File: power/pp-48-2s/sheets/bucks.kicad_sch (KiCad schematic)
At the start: 38 parts, among them J4 12V AUX OUT, U1 LM5164DDA, U2 LM5164DDA

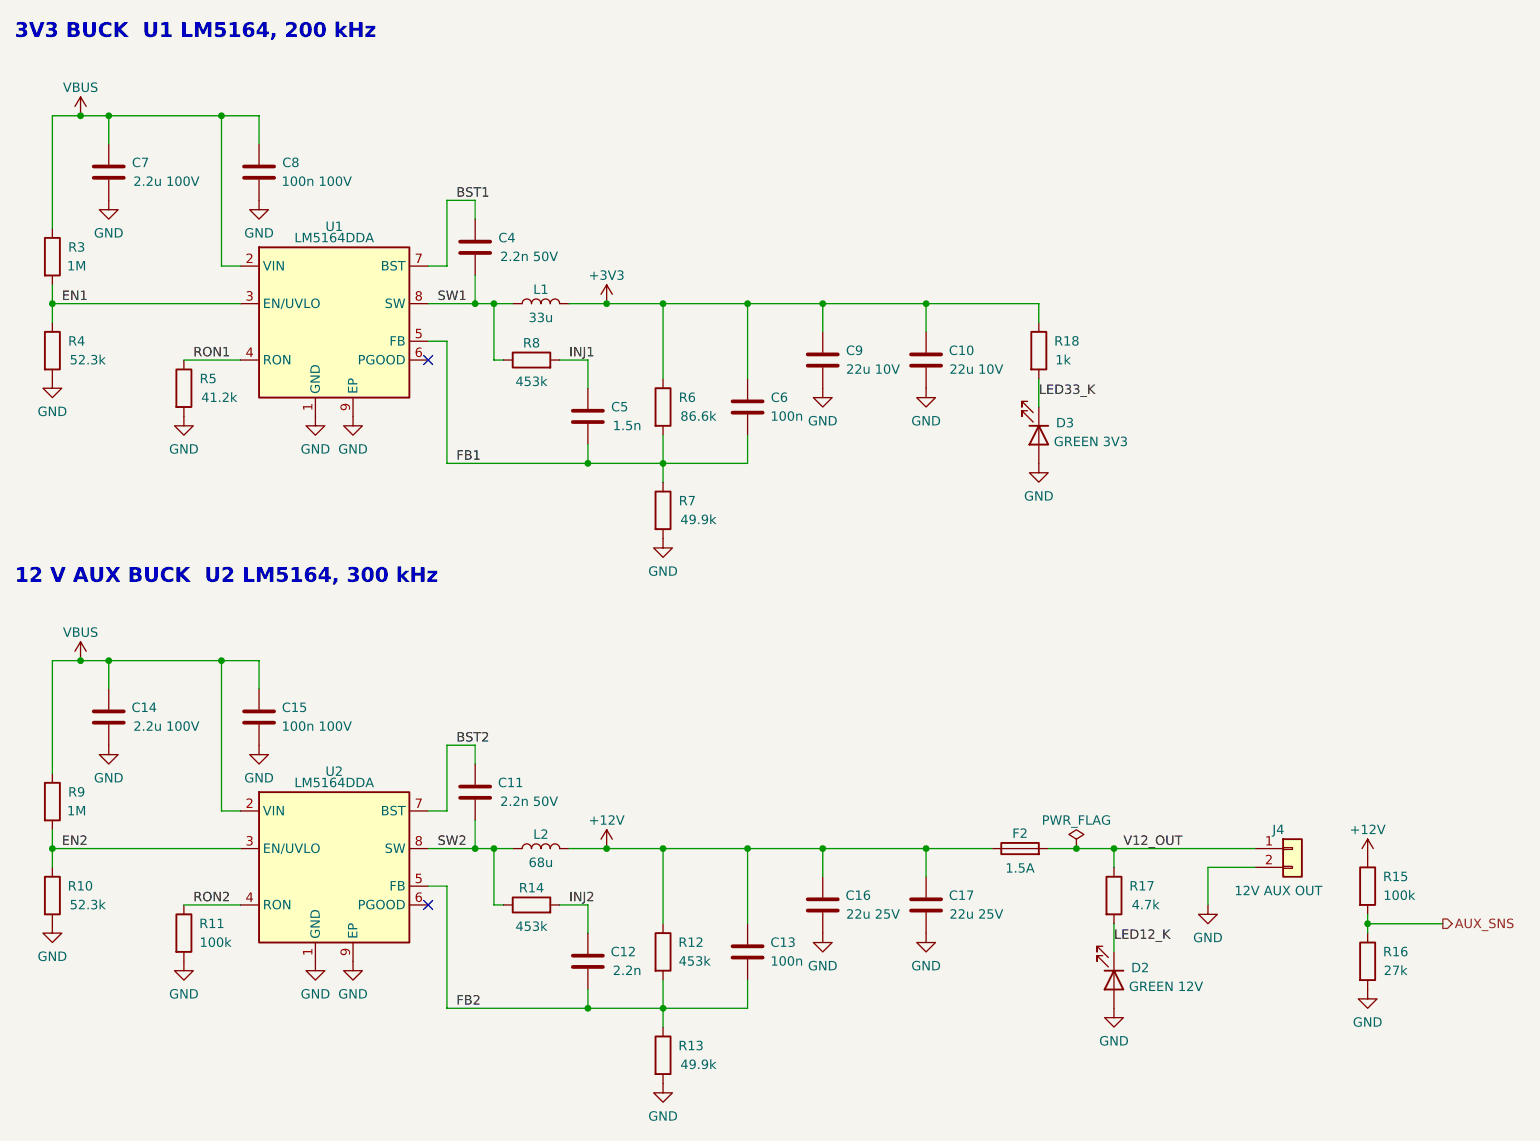
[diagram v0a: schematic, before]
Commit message: power: PP-48-2S four fixes: LED polarity, LM5164 ripple network, latch clear driver, brick sense checked
LEDs: Device:LED pin 1 is K; every LED had the resistor on pin 1 and
GND on pin 2. Nets swapped (LEDnn_K -> LEDnn_A), footprints turned 180
degrees (plan 80). Ripple injection: TI SNVSAU4D Table 6-1 / Fig 7-1
have CA node -> VOUT and CB node -> FB; tables fixed, C5/C6 and
C12/C13 swapped places and rewired on the board (plans 81, 82). Latch
clear: Sn_LCLR now drives the Q104/Q204 gate (+ R112/R212); the latch
node is /Slot n/CLRN (plans 81, 83). Brick SENSE+/-: the PM-19V-200W
module leaves pins 5-7 unconnected, X1.5/X1.7 stay NC.
ERC 0; schcheck shows exactly the intended pin changes; board relinked
with pcbkit relink --allow-shorts and hand-fixed; gndpour, silk,
connlabels re-run; DRC 5 warnings as before, 0 unconnected.
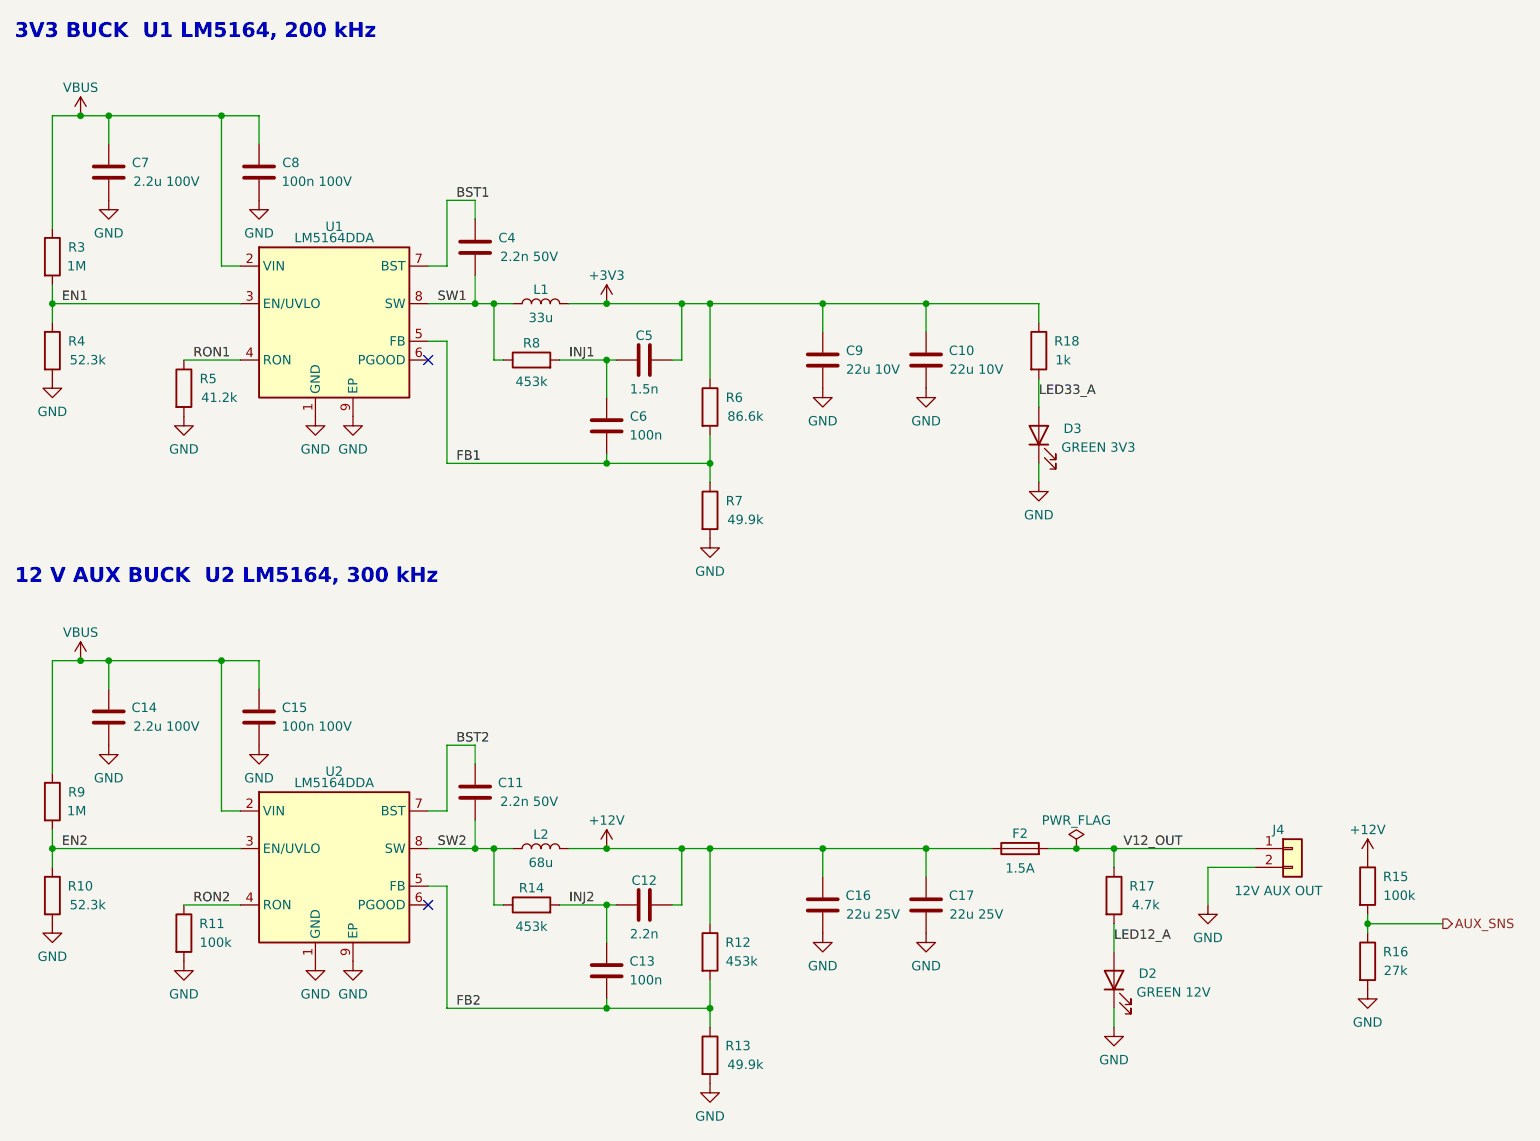
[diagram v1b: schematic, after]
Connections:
- net +12V: now also C12.2; no longer C13.2
- net +3V3: now also C5.2; no longer C6.2
- net FB1: now also C6.2; no longer C5.2, C6.1
- net FB2: now also C13.2; no longer C12.2, C13.1
- net GND: now also D2.1 (K), D3.1 (K); no longer D2.2 (A), D3.2 (A)
- net INJ1: now also C6.1
- net INJ2: now also C13.1
- net LED12_K renamed LED12_A
- net LED12_A: now also D2.2 (A); no longer D2.1 (K)
- net LED33_K renamed LED33_A
- net LED33_A: now also D3.2 (A); no longer D3.1 (K)
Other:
- moved on the sheet: C12, C13, C5, C6, D2, D3, R12, R13, R6, R7

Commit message: power: PP-48-2S L2 Bourns SRR1260-680M (0 at LCSC) -> Sumida CDRH127/LDNP-680MC C2452974; datasheet land pattern equals the 12x12 footprint pads
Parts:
- L2: LCSC (none) -> C2452974; MPN Bourns SRR1260-680M -> Sumida CDRH127/LDNP-680MC
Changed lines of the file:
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@@
 			)
 		)
-		(property "Description" "shielded, Isat >= 1.5 A (Bourns SRR1260 class)"
+		(property "Description" "shielded, Isat >= 1.5 A, 12x12 land pattern (SRR1260 / CDRH127 class)"
 			(at 85.09 53.34 0)
 			(hide yes)
@@
 			)
 		)
-		(property "Description" "shielded, Isat >= 1.5 A (Bourns SRR1260 class)"
+		(property "Description" "shielded, Isat >= 1.5 A, 12x12 land pattern (SRR1260 / CDRH127 class)"
 			(at 85.09 127 0)
 			(hide yes)
@@
 			)
 		)
-		(property "LCSC" ""
+		(property "LCSC" "C2452974"
 			(at 85.09 127 0)
 			(hide yes)
@@
 			)
 		)
-		(property "MPN" "Bourns SRR1260-680M"
+		(property "MPN" "Sumida CDRH127/LDNP-680MC"
 			(at 85.09 127 0)
 			(hide yes)
